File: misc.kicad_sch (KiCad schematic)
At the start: 39 parts, among them J2 Tag-Connect_TC2030-IDC-NL_2x3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, U1 MPFS250T-FCVG484, U2 SDINBDG4-8G, U3 MT25QL01GBBB1EW9-0SIT

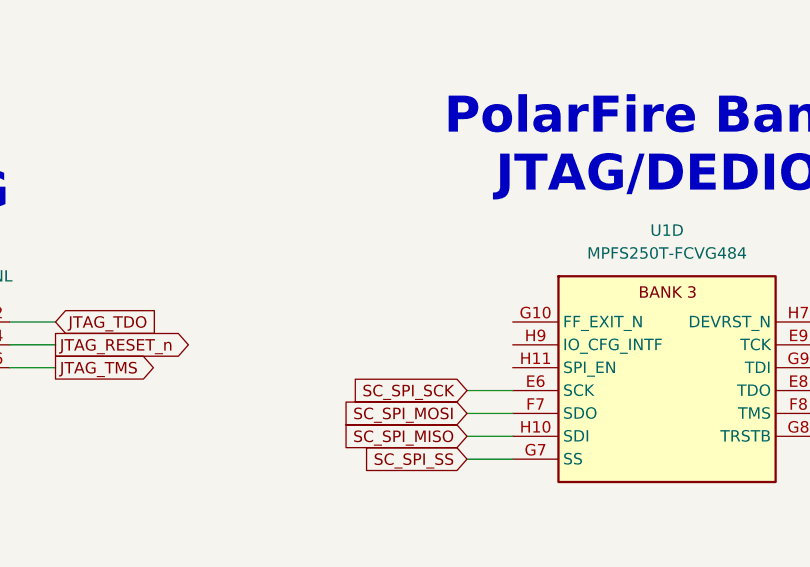
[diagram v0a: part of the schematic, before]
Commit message: [#54899] Add pull-up resistors to Bank 3 of MPFS250T
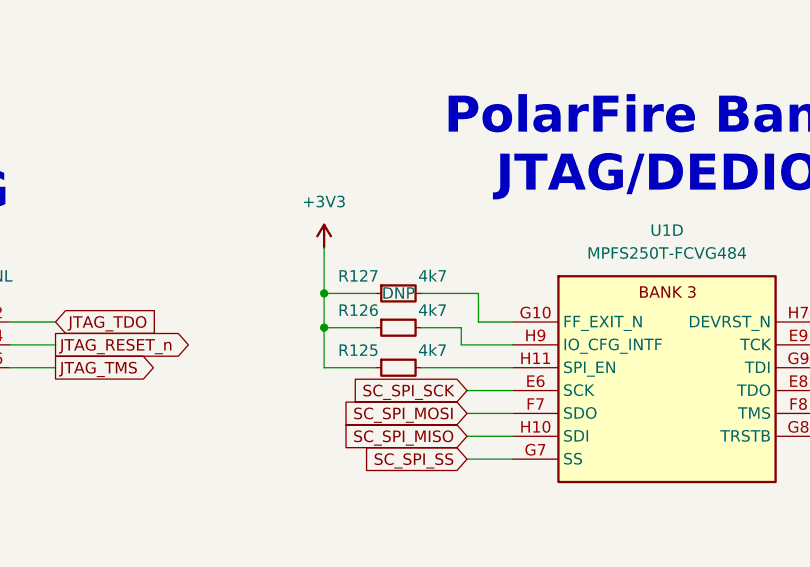
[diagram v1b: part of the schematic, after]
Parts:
- added R125, R126, R127: R_4k7_0402, antmicro-footprints:R_0402_1005Metric, symbol antmicroResistors0402:R_4k7_0402
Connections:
- net +3V3: now also R125.1, R126.1, R127.1
- net at U1.G10 (FF_EXIT_N): now also R127.2
- net at U1.H11 (SPI_EN): now also R125.2
- net at U1.H9 (IO_CFG_INTF): now also R126.2

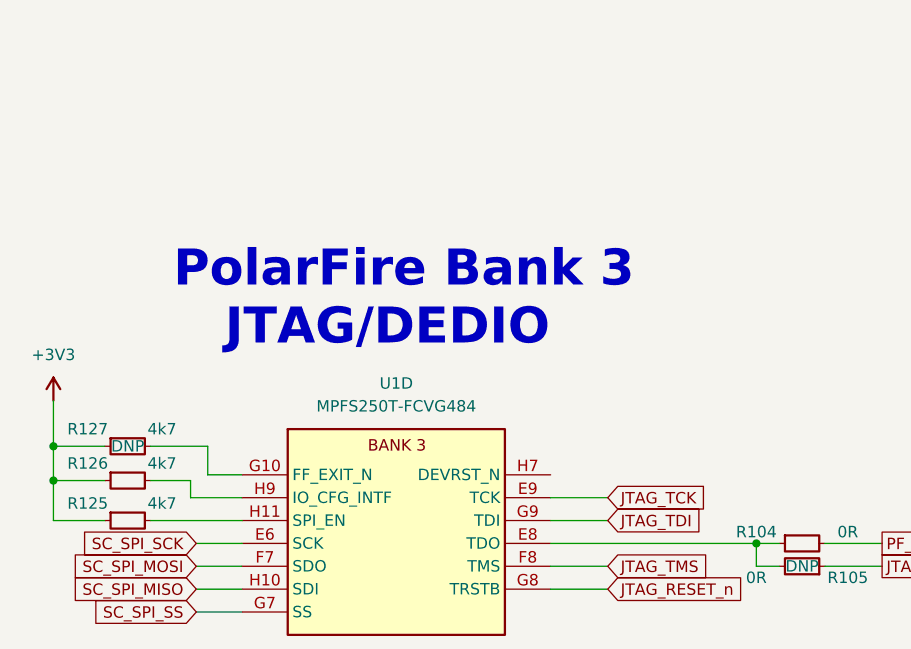
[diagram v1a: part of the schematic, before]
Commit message: [#54899] Add R128
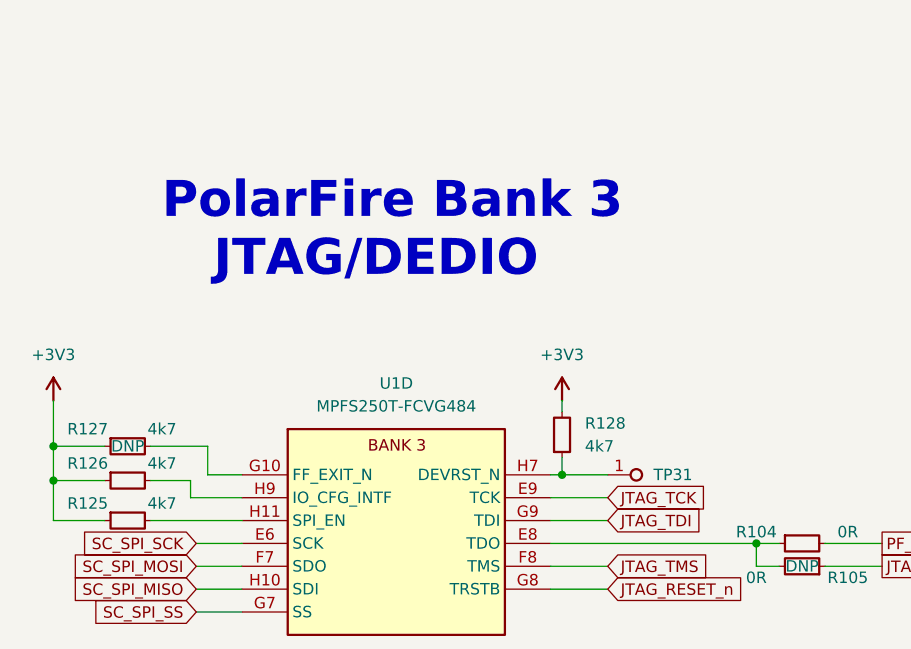
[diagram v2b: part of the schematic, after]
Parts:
- added R128: R_4k7_0402, antmicro-footprints:R_0402_1005Metric, symbol antmicroResistors0402:R_4k7_0402
- added TP31: TP_0.75mm_SMD, antmicro-footprints:TP_SMD_0.75mm, symbol antmicroTestPoints:TP_0.75mm_SMD
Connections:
- net +3V3: now also R128.2
- net at U1.H7 (DEVRST_N): now also R128.1, TP31.1
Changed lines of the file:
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@@
   (junction (at 259.08 173.99) (diameter 0) (color 0 0 0 0)
   )
+  (junction (at 353.06 74.93) (diameter 0) (color 0 0 0 0)
+  )
   (junction (at 219.71 200.66) (diameter 0) (color 0 0 0 0)
   )
@@
     (stroke (width 0) (type default))
   )
+  (wire (pts (xy 353.06 74.93) (xy 358.14 74.93))
+    (stroke (width 0) (type default))
+  )
   (wire (pts (xy 351.79 77.47) (xy 358.14 77.47))
     (stroke (width 0) (type default))
@@
     (stroke (width 0) (type default))
   )
+  (wire (pts (xy 353.06 66.675) (xy 353.06 67.945))
+    (stroke (width 0) (type default))
+  )
   (wire (pts (xy 296.545 75.565) (xy 296.545 80.01))
     (stroke (width 0) (type default))
@@
     (stroke (width 0) (type default))
   )
+  (wire (pts (xy 353.06 73.025) (xy 353.06 74.93))
+    (stroke (width 0) (type default))
+  )
   (wire (pts (xy 269.24 173.99) (xy 269.24 179.07))
     (stroke (width 0) (type default))
@@
     (stroke (width 0) (type default))
   )
+  (wire (pts (xy 351.79 74.93) (xy 353.06 74.93))
+    (stroke (width 0) (type default))
+  )
   (wire (pts (xy 296.545 80.01) (xy 302.26 80.01))
     (stroke (width 0) (type default))
@@
     (effects (font (size 4 4) (thickness 0.8) bold) (justify left bottom))
   )
-  (text "PolarFire Bank 3\n   JTAG/DEDIO" (at 309.88 60.96 0)
+  (text "PolarFire Bank 3\n   JTAG/DEDIO" (at 308.61 53.34 0)
     (effects (font (size 4 4) (thickness 0.8) bold) (justify left bottom))
   )
@@
     )
   )
+  (symbol (lib_id "antmicroTestPoints:TP_0.75mm_SMD") (at 358.14 74.93 0) (unit 1)
+    (in_bom no) (on_board yes) (dnp no) (fields_autoplaced)
+    (property "Reference" "TP31" (at 363.22 74.93 0)
+      (effects (font (size 1.27 1.27) (thickness 0.15)) (justify left))
+    )
+    (property "Value" "TP_0.75mm_SMD" (at 368.935 78.74 0)
+      (effects (font (size 1.27 1.27) (thickness 0.15)) (justify left bottom) hide)
+    )
+    (property "Footprint" "antmicro-footprints:TP_SMD_0.75mm" (at 368.935 81.28 0)
+      (effects (font (size 1.27 1.27) (thickness 0.15)) (justify left bottom) hide)
+    )
+    (property "Datasheet" "" (at 375.92 87.63 0)
+      (effects (font (size 1.27 1.27) (thickness 0.15)) (justify left bottom) hide)
+    )
+    (property "MPN" "" (at 368.935 86.36 0)
+      (effects (font (size 1.27 1.27) (thickness 0.15)) (justify left bottom) hide)
+    )
+    (property "Manufacturer" "" (at 368.935 81.28 0)
+      (effects (font (size 1.27 1.27) (thickness 0.15)) (justify left bottom) hide)
+    )
+    (property "Author" "Antmicro" (at 368.935 83.82 0)
+      (effects (font (size 1.27 1.27) (thickness 0.15)) (justify left bottom) hide)
+    )
+    (property "License" "Apache-2.0" (at 368.935 86.36 0)
+      (effects (font (size 1.27 1.27) (thickness 0.15)) (justify left bottom) hide)
+    )
+    (pin "1")
+    (instances
+      (project "polarfire-som"
+        (path "/db4a0d3e-2eb3-499e-977d-6eb378cfd3ed/6b5c9386-08fc-46bf-a582-c320c1d104da"
+          (reference "TP31") (unit 1)
+        )
+      )
+    )
+  )
   (symbol (lib_id "antmicroResistors0402:R_0R_0402") (at 382.27 85.09 180) (unit 1)
     (in_bom no) (on_board yes) (dnp no)
@@
     )
   )
+  (symbol (lib_id "antmicroResistors0402:R_4k7_0402") (at 353.06 73.025 90) (unit 1)
+    (in_bom yes) (on_board yes) (dnp no) (fields_autoplaced)
+    (property "Reference" "R128" (at 355.6 69.215 90)
+      (effects (font (size 1.27 1.27) (thickness 0.15)) (justify right))
+    )
+    (property "Value" "R_4k7_0402" (at 365.76 52.705 0)
+      (effects (font (size 1.27 1.27) (thickness 0.15)) (justify left bottom) hide)
+    )
+    (property "Footprint" "antmicro-footprints:R_0402_1005Metric" (at 368.3 52.705 0)
+      (effects (font (size 1.27 1.27) (thickness 0.15)) (justify left bottom) hide)
+    )
+    (property "Datasheet" "https://www.bourns.com/docs/product-datasheets/cr.pdf" (at 370.84 52.705 0)
+      (effects (font (size 1.27 1.27) (thickness 0.15)) (justify left bottom) hide)
+    )
+    (property "MPN" "CR0402-FX-4701GLF" (at 373.38 52.705 0)
+      (effects (font (size 1.27 1.27) (thickness 0.15)) (justify left bottom) hide)
+    )
+    (property "Manufacturer" "Bourns" (at 375.92 52.705 0)
+      (effects (font (size 1.27 1.27) (thickness 0.15)) (justify left bottom) hide)
+    )
+    (property "License" "Apache-2.0" (at 378.46 52.705 0)
+      (effects (font (size 1.27 1.27) (thickness 0.15)) (justify left bottom) hide)
+    )
+    (property "Author" "Antmicro" (at 381 52.705 0)
+      (effects (font (size 1.27 1.27) (thickness 0.15)) (justify left bottom) hide)
+    )
+    (property "Val" "4k7" (at 355.6 71.755 90)
+      (effects (font (size 1.27 1.27) (thickness 0.15)) (justify right))
+    )
+    (property "Tolerance" "1%" (at 363.22 52.705 0)
+      (effects (font (size 1.27 1.27)) (justify left bottom) hide)
+    )
+    (pin "1")
+    (pin "2")
+    (instances
+      (project "polarfire-som"
+        (path "/db4a0d3e-2eb3-499e-977d-6eb378cfd3ed/6b5c9386-08fc-46bf-a582-c320c1d104da"
+          (reference "R128") (unit 1)
+        )
+      )
+    )
+  )
   (symbol (lib_id "antmicroMemory:SDINBDG4-8G") (at 222.25 190.5 0) (unit 1)
     (in_bom yes) (on_board yes) (dnp no) (fields_autoplaced)
@@
         )
       )
+    )
+  )
+  (symbol (lib_id "antmicropower:+3V3") (at 353.06 66.675 0) (unit 1)
+    (in_bom yes) (on_board yes) (dnp no) (fields_autoplaced)
+    (property "Reference" "#PWR032" (at 368.3 69.215 0)
+      (effects (font (size 1.27 1.27) (thickness 0.15)) (justify left bottom) hide)
+    )
+    (property "Value" "+3V3" (at 353.06 61.595 0)
+      (effects (font (size 1.27 1.27) (thickness 0.15)))
+    )
+    (property "Footprint" "" (at 368.3 74.295 0)
+      (effects (font (size 1.27 1.27) (thickness 0.15)) (justify left bottom) hide)
+    )
+    (property "Datasheet" "" (at 368.3 76.835 0)
+      (effects (font (size 1.27 1.27) (thickness 0.15)) (justify left bottom) hide)
+    )
+    (property "Author" "Antmicro" (at 368.3 74.295 0)
+      (effects (font (size 1.27 1.27) (thickness 0.15)) (justify left bottom) hide)
+    )
+    (property "License" "Apache-2.0" (at 368.3 76.835 0)
+      (effects (font (size 1.27 1.27) (thickness 0.15)) (justify left bottom) hide)
+    )
+    (pin "1")
+    (instances
+      (project "polarfire-som"
+        (path "/db4a0d3e-2eb3-499e-977d-6eb378cfd3ed/6b5c9386-08fc-46bf-a582-c320c1d104da"
+          (reference "#PWR032") (unit 1)
+        )
+      )

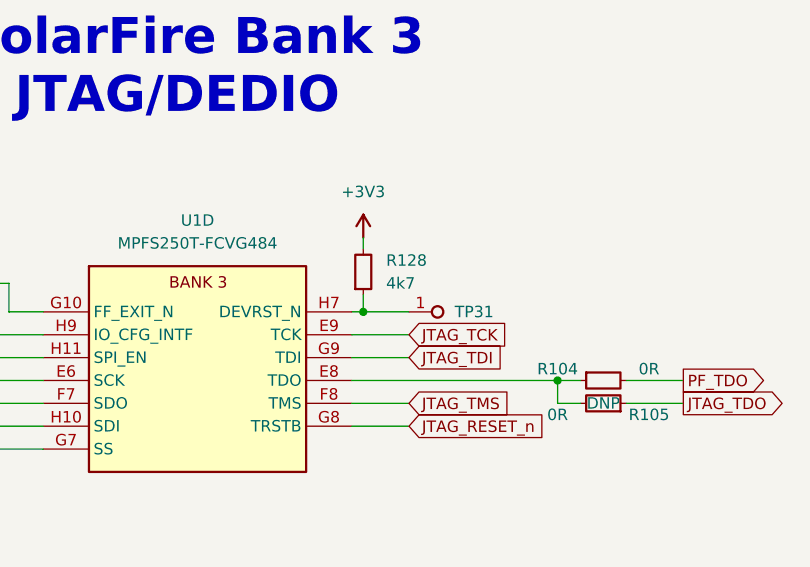
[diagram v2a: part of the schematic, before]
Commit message: [#54899] Change value of R128 from 4k7 to 1k
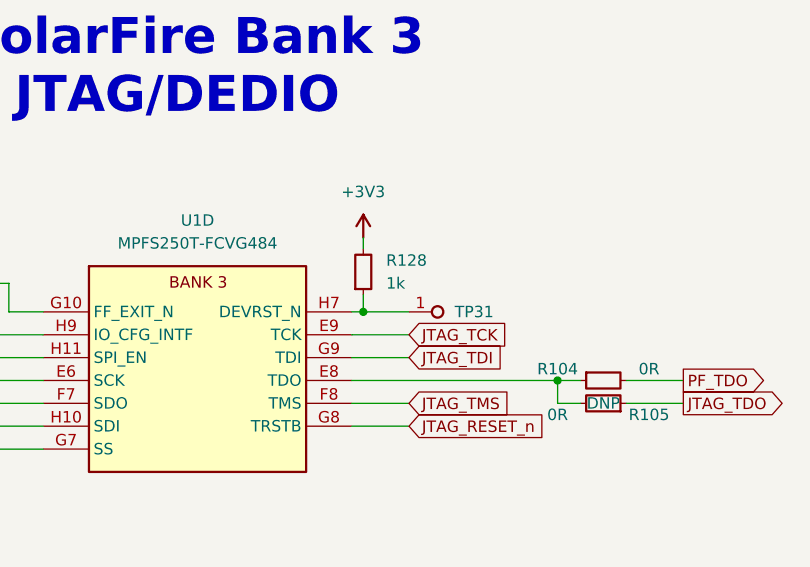
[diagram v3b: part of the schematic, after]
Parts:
- removed R128: R_4k7_0402, antmicro-footprints:R_0402_1005Metric, symbol antmicroResistors0402:R_4k7_0402
- added R128: R_1k_0402, antmicro-footprints:R_0402_1005Metric, symbol antmicroResistors0402:R_1k_0402
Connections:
- net +3V3: now also R128.2
- net at TP31.1, U1.H7 (DEVRST_N): now also R128.1
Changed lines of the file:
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@@
+    )
+  )
+  (symbol (lib_id "antmicroResistors0402:R_1k_0402") (at 353.06 73.025 90) (unit 1)
+    (in_bom yes) (on_board yes) (dnp no) (fields_autoplaced)
+    (property "Reference" "R128" (at 355.6 69.215 90)
+      (effects (font (size 1.27 1.27) (thickness 0.15)) (justify right))
+    )
+    (property "Value" "R_1k_0402" (at 365.76 52.705 0)
+      (effects (font (size 1.27 1.27) (thickness 0.15)) (justify left bottom) hide)
+    )
+    (property "Footprint" "antmicro-footprints:R_0402_1005Metric" (at 368.3 52.705 0)
+      (effects (font (size 1.27 1.27) (thickness 0.15)) (justify left bottom) hide)
+    )
+    (property "Datasheet" "https://www.bourns.com/docs/product-datasheets/cr.pdf" (at 370.84 52.705 0)
+      (effects (font (size 1.27 1.27) (thickness 0.15)) (justify left bottom) hide)
+    )
+    (property "MPN" "CR0402-FX-1001GLF" (at 373.38 52.705 0)
+      (effects (font (size 1.27 1.27) (thickness 0.15)) (justify left bottom) hide)
+    )
+    (property "Manufacturer" "Bourns" (at 375.92 52.705 0)
+      (effects (font (size 1.27 1.27) (thickness 0.15)) (justify left bottom) hide)
+    )
+    (property "License" "Apache-2.0" (at 378.46 52.705 0)
+      (effects (font (size 1.27 1.27) (thickness 0.15)) (justify left bottom) hide)
+    )
+    (property "Author" "Antmicro" (at 381 52.705 0)
+      (effects (font (size 1.27 1.27) (thickness 0.15)) (justify left bottom) hide)
+    )
+    (property "Val" "1k" (at 355.6 71.755 90)
+      (effects (font (size 1.27 1.27) (thickness 0.15)) (justify right))
+    )
+    (property "Tolerance" "1%" (at 363.22 52.705 0)
+      (effects (font (size 1.27 1.27)) (justify left bottom) hide)
+    )
+    (pin "2")
+    (pin "1")
+    (instances
+      (project "polarfire-som"
+        (path "/db4a0d3e-2eb3-499e-977d-6eb378cfd3ed/6b5c9386-08fc-46bf-a582-c320c1d104da"
+          (reference "R128") (unit 1)
+        )
+      )
     )
   )
@@
         )
       )
-    )
-  )
-  (symbol (lib_id "antmicroResistors0402:R_4k7_0402") (at 353.06 73.025 90) (unit 1)
-    (in_bom yes) (on_board yes) (dnp no) (fields_autoplaced)
-    (property "Reference" "R128" (at 355.6 69.215 90)
-      (effects (font (size 1.27 1.27) (thickness 0.15)) (justify right))
-    )
-    (property "Value" "R_4k7_0402" (at 365.76 52.705 0)
-      (effects (font (size 1.27 1.27) (thickness 0.15)) (justify left bottom) hide)
-    )
-    (property "Footprint" "antmicro-footprints:R_0402_1005Metric" (at 368.3 52.705 0)
-      (effects (font (size 1.27 1.27) (thickness 0.15)) (justify left bottom) hide)
-    )
-    (property "Datasheet" "https://www.bourns.com/docs/product-datasheets/cr.pdf" (at 370.84 52.705 0)
-      (effects (font (size 1.27 1.27) (thickness 0.15)) (justify left bottom) hide)
-    )
-    (property "MPN" "CR0402-FX-4701GLF" (at 373.38 52.705 0)
-      (effects (font (size 1.27 1.27) (thickness 0.15)) (justify left bottom) hide)
-    )
-    (property "Manufacturer" "Bourns" (at 375.92 52.705 0)
-      (effects (font (size 1.27 1.27) (thickness 0.15)) (justify left bottom) hide)
-    )
-    (property "License" "Apache-2.0" (at 378.46 52.705 0)
-      (effects (font (size 1.27 1.27) (thickness 0.15)) (justify left bottom) hide)
-    )
-    (property "Author" "Antmicro" (at 381 52.705 0)
-      (effects (font (size 1.27 1.27) (thickness 0.15)) (justify left bottom) hide)
-    )
-    (property "Val" "4k7" (at 355.6 71.755 90)
-      (effects (font (size 1.27 1.27) (thickness 0.15)) (justify right))
-    )
-    (property "Tolerance" "1%" (at 363.22 52.705 0)
-      (effects (font (size 1.27 1.27)) (justify left bottom) hide)
-    )
-    (pin "1")
-    (pin "2")
-    (instances
-      (project "polarfire-som"
-        (path "/db4a0d3e-2eb3-499e-977d-6eb378cfd3ed/6b5c9386-08fc-46bf-a582-c320c1d104da"
-          (reference "R128") (unit 1)
-        )
-      )

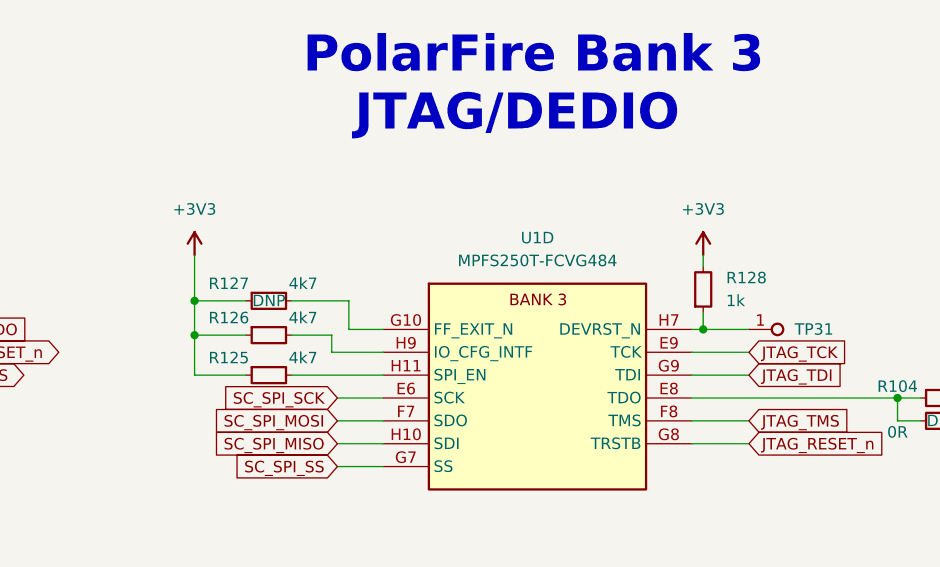
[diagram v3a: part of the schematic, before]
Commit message: [#54899] Clean duplicated components
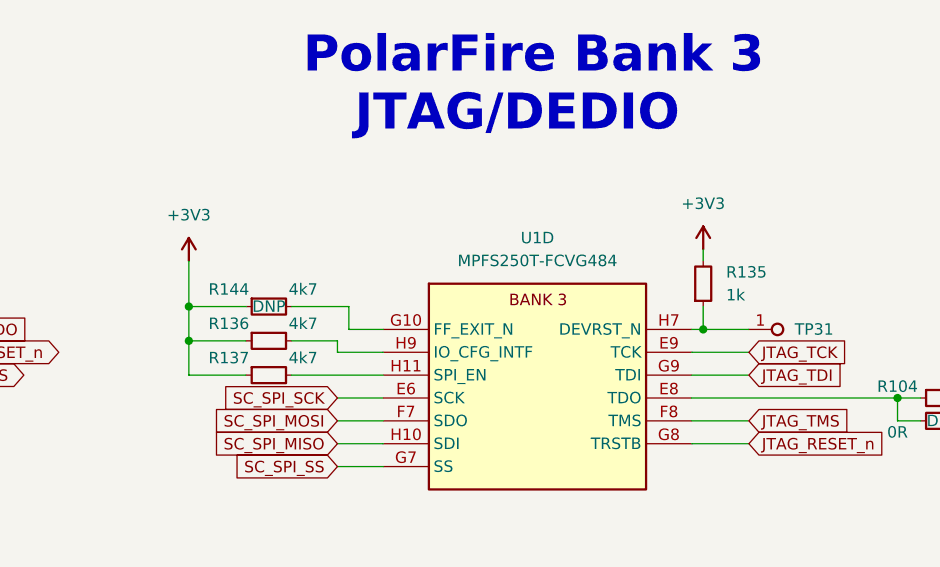
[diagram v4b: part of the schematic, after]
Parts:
- removed R125, R126, R127: R_4k7_0402, antmicro-footprints:R_0402_1005Metric, symbol antmicroResistors0402:R_4k7_0402
- removed R128: R_1k_0402, antmicro-footprints:R_0402_1005Metric, symbol antmicroResistors0402:R_1k_0402
- added R135: R_1k_0402, antmicro-footprints:R_0402_1005Metric, symbol antmicroResistors0402:R_1k_0402
- added R136, R137, R144: R_4k7_0402, antmicro-footprints:R_0402_1005Metric, symbol antmicroResistors0402:R_4k7_0402
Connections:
- net +3V3: now also R135.2, R136.1, R137.1, R144.1
- net at TP31.1, U1.H7 (DEVRST_N): now also R135.1
- net at U1.H11 (SPI_EN): now also R137.2
- net at U1.H9 (IO_CFG_INTF): now also R136.2
- net at U1.G10 (FF_EXIT_N): now also R144.2

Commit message: [#54899] Re-annotate components
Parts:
- renumbered R17 to R22, R18 to R23, R19 to R24, R20 to R25, R21 to R26, R22 to R27, R23 to R28, R24 to R29, R25 to R30, R26 to R31, R27 to R32, R28 to R33, R29 to R34, R30 to R35, R31 to R36, R32 to R37, R33 to R38, R144 to R39, R136 to R40, R137 to R41, R135 to R42, R104 to R43, R105 to R44, R121 to R45, R122 to R46, TP31 to TP1
